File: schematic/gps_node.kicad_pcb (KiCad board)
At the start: 2 copper layers, 48 x 75 mm, 77 parts, among them IC2 MCP73831/2, J1 USB_OTG, J10 Mounting Hole, J11 TEST Vbatt, J12 Test 3.3v, J13 Test Gnd, J14 UART RF, J15 I2C GPS, J16 UART GPS, J17 GPIO_0, J18 GPIO_1, J2 AVR ICSP, J3 LIPO_BAT, J4 SOLAR, J5 FW_UPDATE, J6 SMA, J7 Mounting Hole, J8 Mounting Hole, J9 Mounting Hole, SW1 SW_SP3T, SW2 RESET, U1 TLV71333PDBV, U2 ublox-cam-m8q-0, U3 ATMEGA32U4-AU, U4 RN2483, Y1 16MHz

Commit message: First round of layout done
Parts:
- added IC1: MMA8452Q, gps_node_components:MMA8452Q, F.Cu at (124.7, 99.3)
- C10, C13, C20, C3, D1, D2, D5, F1, R1, R16, R17, R18, R19, R2: moved to B.Cu
- moved R19 98.9 mm to (128.3, 71.9), turned to 90 degrees
- moved C5 96.1 mm to (111.8, 95.8), turned to 270 degrees
- moved R10 94.6 mm to (121.9, 80.0)
- moved J12 93.3 mm to (109.2, 83.8)
- moved R18 93.1 mm to (131.3, 71.9), turned to 90 degrees
- moved R4 92.6 mm to (110.5, 80.3), turned to 90 degrees
- moved R3 89.5 mm to (112.5, 80.3), turned to 90 degrees
- moved C2 87.4 mm to (111.3, 108.0), turned to 90 degrees
- moved D8 87.2 mm to (115.6, 100.3), turned to 90 degrees
- moved D3 86.9 mm to (113.0, 90.2), turned to 90 degrees
- moved D7 85.5 mm to (113.8, 100.3), turned to 90 degrees
- moved J11 85.3 mm to (111.8, 116.8)
- moved C6 85.2 mm to (138.9, 85.1), turned to 270 degrees
- moved D2 84.7 mm to (108.7, 93.7), turned to 180 degrees
- moved D1 84.5 mm to (109.0, 87.4), turned to 90 degrees
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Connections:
- C18 pad 1: (no net) -> Net-(C18-Pad1)
- R16 pad 1: (no net) -> +BATT
- R8 pad 2: (no net) -> Net-(IC1-Pad9)
- R9 pad 2: (no net) -> Net-(IC1-Pad11)
- U4 pad 21: Net-(U4-Pad21) -> GND
- U4 pad 22: Net-(U4-Pad21) -> GND
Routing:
- net GND: track 0.00 -> 444.7 mm, vias 0 -> 43
- net +3V3: track 0.00 -> 187.8 mm, vias 0 -> 9
- net /I2C_GPS_SCL: track 0.00 -> 115.0 mm, vias 0 -> 2
- net /I2C_GPS_SDA: track 0.00 -> 106.0 mm, vias 0 -> 2
- net /UART_AT_TO_RN: track 0.00 -> 76.1 mm, vias 0 -> 3
- net /UART_RN_TO_AT: track 0.00 -> 70.9 mm, vias 0 -> 3
- net /UART_GPS_OUT: track 0.00 -> 65.8 mm, vias 0 -> 2
- net +BATT: track 0.00 -> 64.2 mm, vias 0 -> 3
- net /UART_GPS_IN: track 0.00 -> 61.6 mm
- net /MCU_PWSEL11_IN: track 0.00 -> 48.4 mm, vias 0 -> 3
- net /MCU_PWSEL0_IN: track 0.00 -> 46.2 mm, vias 0 -> 3
- net /RESET: track 0.00 -> 43.0 mm, vias 0 -> 1
- net /ACC_INT2: track 0.00 -> 42.6 mm, vias 0 -> 2
- net /MCU__OUT: track 0.00 -> 42.5 mm, vias 0 -> 2
- net /SCK: track 0.00 -> 40.5 mm, vias 0 -> 2
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- added copper zone on B.Cu, net GND
- added copper zone on F.Cu, net GND
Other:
- outline, holes or cut-outs redrawn

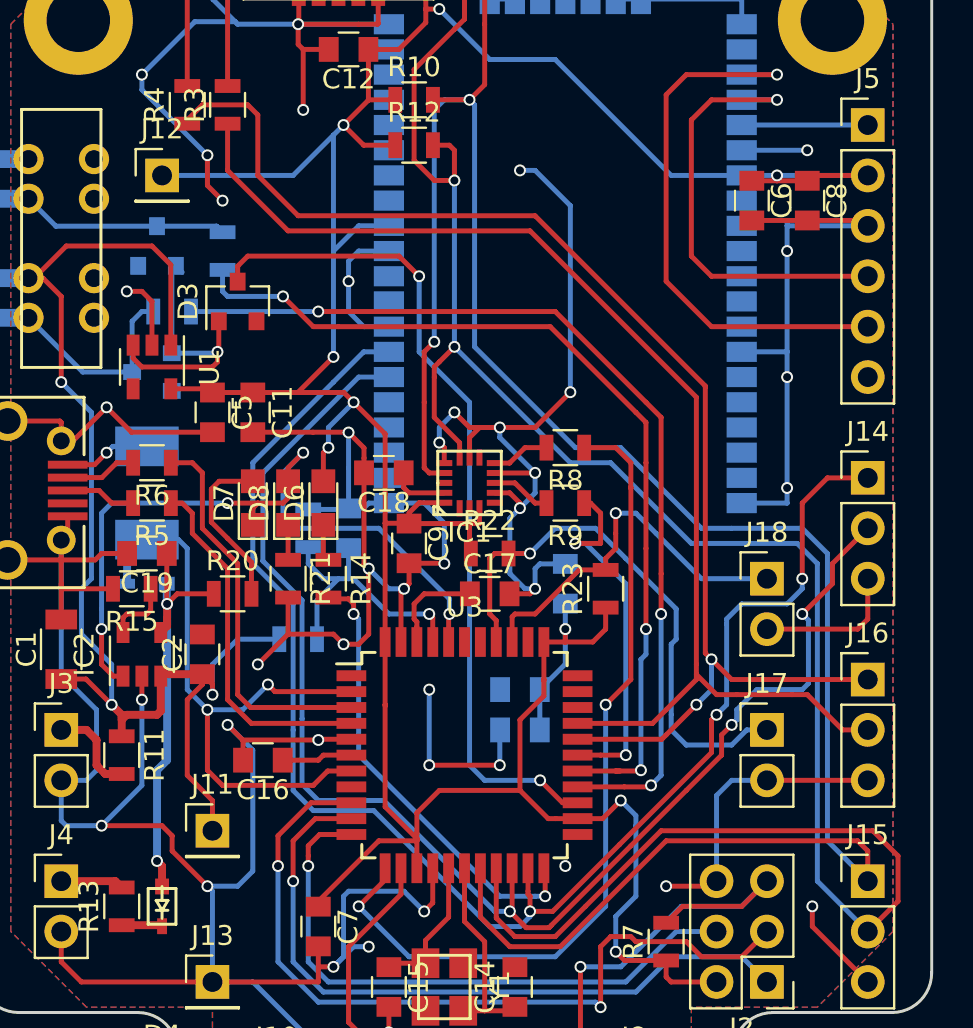
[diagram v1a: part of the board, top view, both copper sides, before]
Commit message: Issue #2: Adds RN2483 reset pin
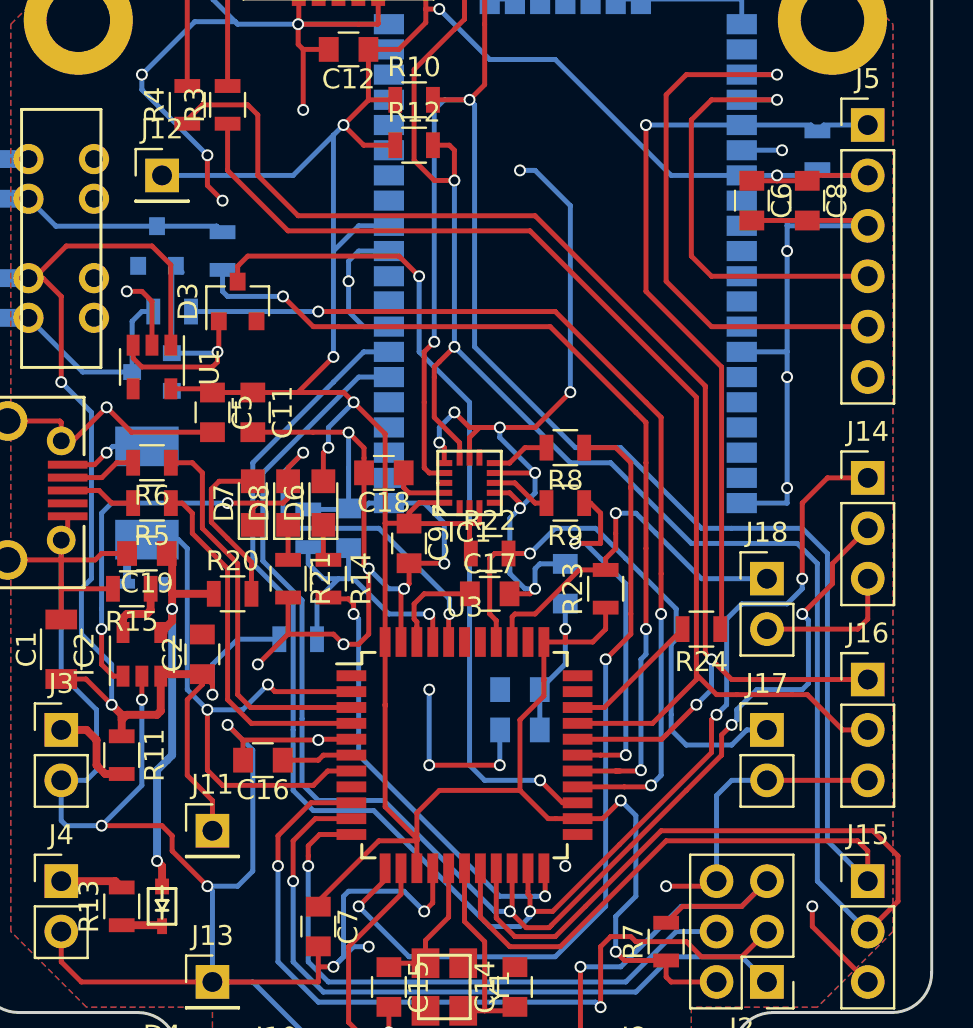
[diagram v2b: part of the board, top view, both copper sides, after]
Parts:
- added R24: 470, Resistors_SMD:R_0805, F.Cu at (136.4, 106.7)
- added R25: 10k, Resistors_SMD:R_0805, B.Cu at (142.2, 82.5)
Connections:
- net Net-(J5-Pad1) renamed /RN_RESET
- U3 pad 31: (no net) -> Net-(R24-Pad2)
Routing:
- net /RN_RESET: track 6.35 -> 38.4 mm, vias 0 -> 1
- net Net-(R24-Pad2): track 0.00 -> 6.92 mm
- net GND: track 444.7 -> 443.5 mm
- net /V_Charger: track 21.7 -> 22.8 mm
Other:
- net class Default: clearance 0.2 -> 0.17
- rule trace_clearance: 0.2 -> 0.17
- rule trace_min: 0.2 -> 0.16

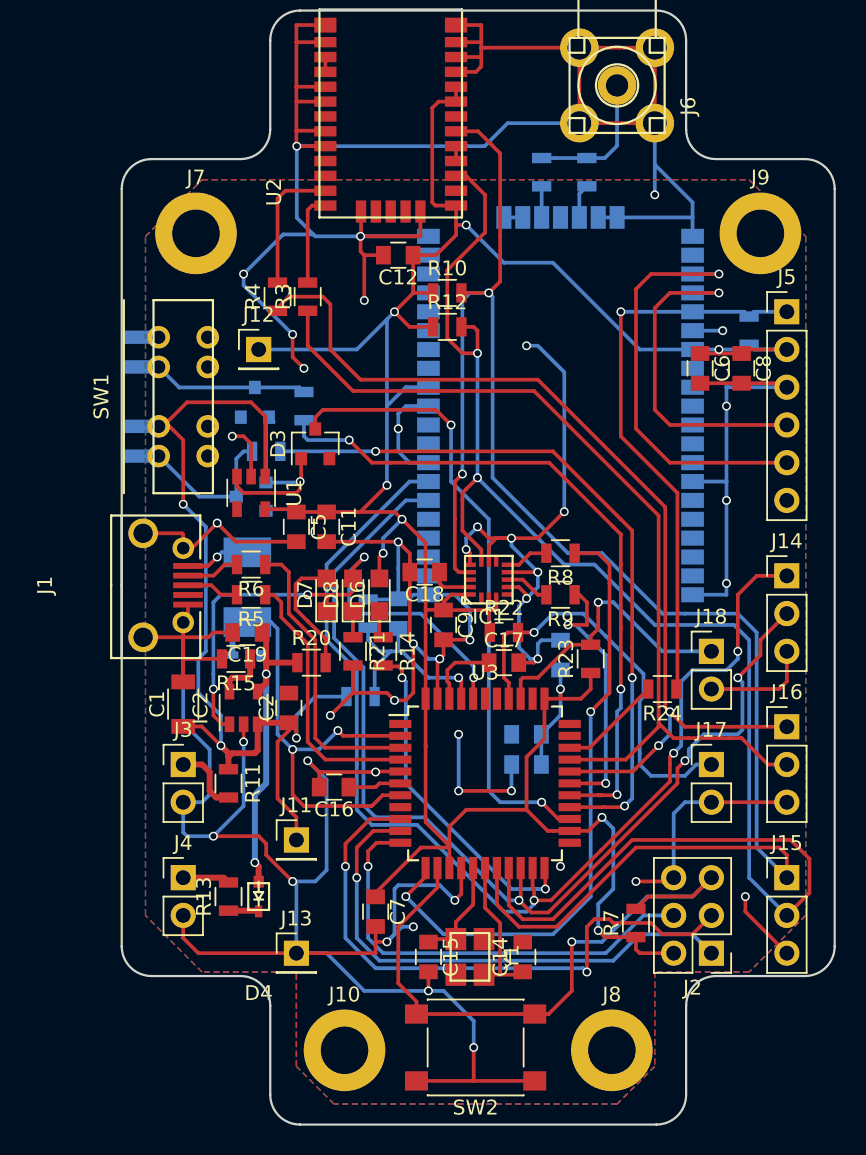
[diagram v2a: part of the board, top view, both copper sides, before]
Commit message: Adds RGB led, updates schematic
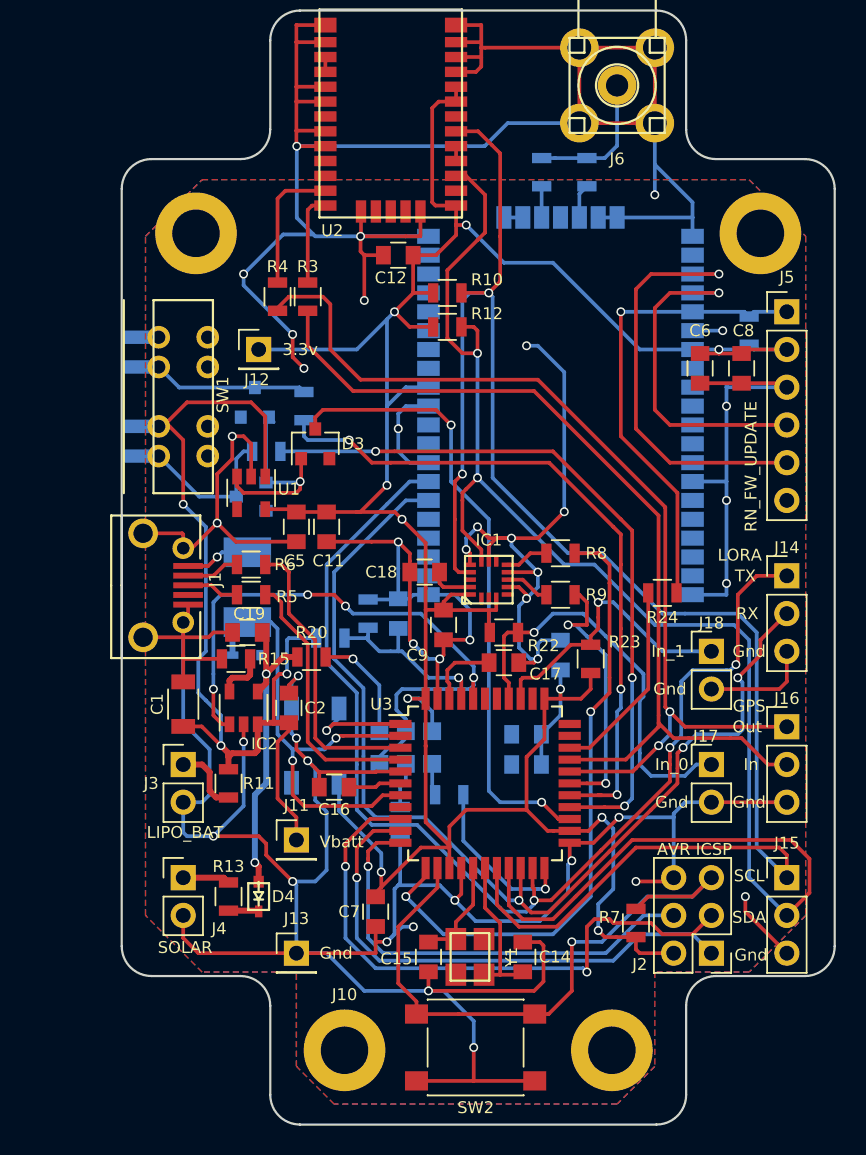
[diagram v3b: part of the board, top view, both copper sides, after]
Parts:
- added LED1: WS2812B, LEDs:LED_WS2812B-PLCC4, B.Cu at (113.0, 110.5)
- D6, D7, D8, R14, R21: moved to B.Cu
- J11: value TEST Vbatt -> Vbatt
- J12: value Test 3.3v -> 3.3v
- J13: value Test Gnd -> Gnd
- J5: value FW_UPDATE -> RN_FW_UPDATE
- moved R21 11.9 mm to (118.7, 115.6)
- moved D8 10.9 mm to (119.1, 110.6)
- moved D6 10.9 mm to (120.9, 110.6)
- moved D7 10.9 mm to (117.3, 110.6)
- moved R14 10.6 mm to (122.0, 113.8), turned to 0 degrees
- moved R24 6.48 mm to (136.4, 100.2)
- moved R16 4.43 mm to (114.0, 103.3)
- moved R20 0.38 mm to (112.8, 104.5)
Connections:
- IC1 pad 13: (no net) -> Net-(IC1-Pad13)
- IC1 pad 15: (no net) -> Net-(IC1-Pad15)
- IC1 pad 16: (no net) -> Net-(IC1-Pad16)
- IC1 pad 3: (no net) -> Net-(IC1-Pad3)
- IC1 pad 8: (no net) -> Net-(IC1-Pad8)
- J1 pad 4: (no net) -> Net-(J1-Pad4)
- J10 pad 1: (no net) -> Net-(J10-Pad1)
- J5 pad 6: (no net) -> Net-(J5-Pad6)
- J7 pad 1: (no net) -> Net-(J7-Pad1)
- J8 pad 1: (no net) -> Net-(J8-Pad1)
- J9 pad 1: (no net) -> Net-(J9-Pad1)
- U1 pad 4: (no net) -> Net-(U1-Pad4)
- U2 pad 2: (no net) -> Net-(U2-Pad2)
- U2 pad 20: (no net) -> Net-(U2-Pad20)
- U2 pad 23: (no net) -> Net-(U2-Pad23)
- U2 pad 24: (no net) -> Net-(U2-Pad24)
- U2 pad 28: (no net) -> Net-(U2-Pad28)
- U2 pad 29: (no net) -> Net-(U2-Pad29)
- U2 pad 30: (no net) -> Net-(U2-Pad30)
- U2 pad 7: (no net) -> Net-(U2-Pad7)
- U3 pad 1: (no net) -> /RGB_LED
- U3 pad 32: (no net) -> Net-(U3-Pad32)
- U3 pad 33: (no net) -> Net-(U3-Pad33)
- U3 pad 38: (no net) -> Net-(U3-Pad38)
- U3 pad 39: (no net) -> Net-(U3-Pad39)
- U3 pad 8: (no net) -> Net-(U3-Pad8)
- U4 pad 10: (no net) -> Net-(U4-Pad10)
- U4 pad 13: (no net) -> Net-(U4-Pad13)
- U4 pad 14: (no net) -> Net-(U4-Pad14)
- U4 pad 15: (no net) -> Net-(U4-Pad15)
- U4 pad 16: (no net) -> Net-(U4-Pad16)
- U4 pad 17: (no net) -> Net-(U4-Pad17)
- U4 pad 18: (no net) -> Net-(U4-Pad18)
- U4 pad 19: (no net) -> Net-(U4-Pad19)
- U4 pad 2: (no net) -> Net-(U4-Pad2)
- U4 pad 29: (no net) -> Net-(U4-Pad29)
- U4 pad 3: (no net) -> Net-(U4-Pad3)
- U4 pad 35: (no net) -> Net-(U4-Pad35)
- U4 pad 36: (no net) -> Net-(U4-Pad36)
- U4 pad 37: (no net) -> Net-(U4-Pad37)
- U4 pad 38: (no net) -> Net-(U4-Pad38)
- U4 pad 39: (no net) -> Net-(U4-Pad39)
- U4 pad 4: (no net) -> Net-(U4-Pad4)
- U4 pad 40: (no net) -> Net-(U4-Pad40)
- U4 pad 42: (no net) -> Net-(U4-Pad42)
- U4 pad 43: (no net) -> Net-(U4-Pad43)
- U4 pad 44: (no net) -> Net-(U4-Pad44)
- U4 pad 45: (no net) -> Net-(U4-Pad45)
- U4 pad 46: (no net) -> Net-(U4-Pad46)
- U4 pad 5: (no net) -> Net-(U4-Pad5)
- U4 pad 9: (no net) -> Net-(U4-Pad9)
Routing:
- net GND: track 443.5 -> 472.3 mm, vias 43 -> 41
- net /LED_OUT: track 22.9 -> 11.4 mm, vias 2 -> 1
- net +3V3: track 188.1 -> 196.2 mm, vias 9 -> 10
- net /RGB_LED: track 0.00 -> 6.98 mm, vias 0 -> 1
- net /RN_RESET: track 38.4 -> 32.0 mm
- net Net-(R24-Pad2): track 6.92 -> 13.4 mm
- net /charge_status: track 38.6 -> 42.8 mm
- net /BAT_MEASURE: track 14.5 -> 12.6 mm
- net +BATT: track 64.2 -> 65.8 mm
- net Net-(D8-Pad1): track 1.76 -> 3.06 mm
- net Net-(D7-Pad2): track 8.37 -> 7.60 mm, vias 0 -> 1
- net (no net): vias 1 -> 0
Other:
- board text added: "GPS"
- board text added: "Gnd"
- board text added: "In"
- board text added: "In_0"
- board text added: "In_1"
- board text added: "LORA"
- board text added: "Out"
- board text added: "RX"
- board text added: "SCL"
- board text added: "SDA"
- board text added: "TX"

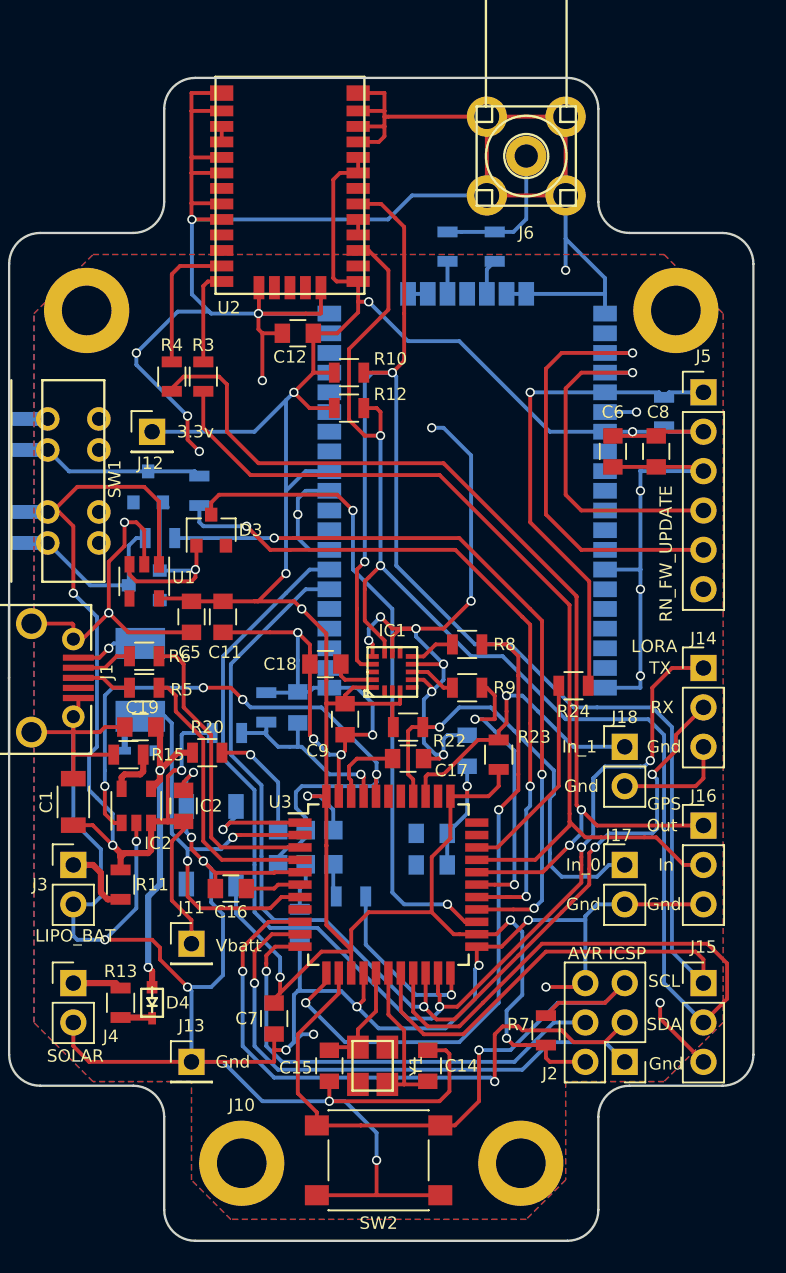
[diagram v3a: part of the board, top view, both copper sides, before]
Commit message: Added more group pour aroudd gps, additional buttons
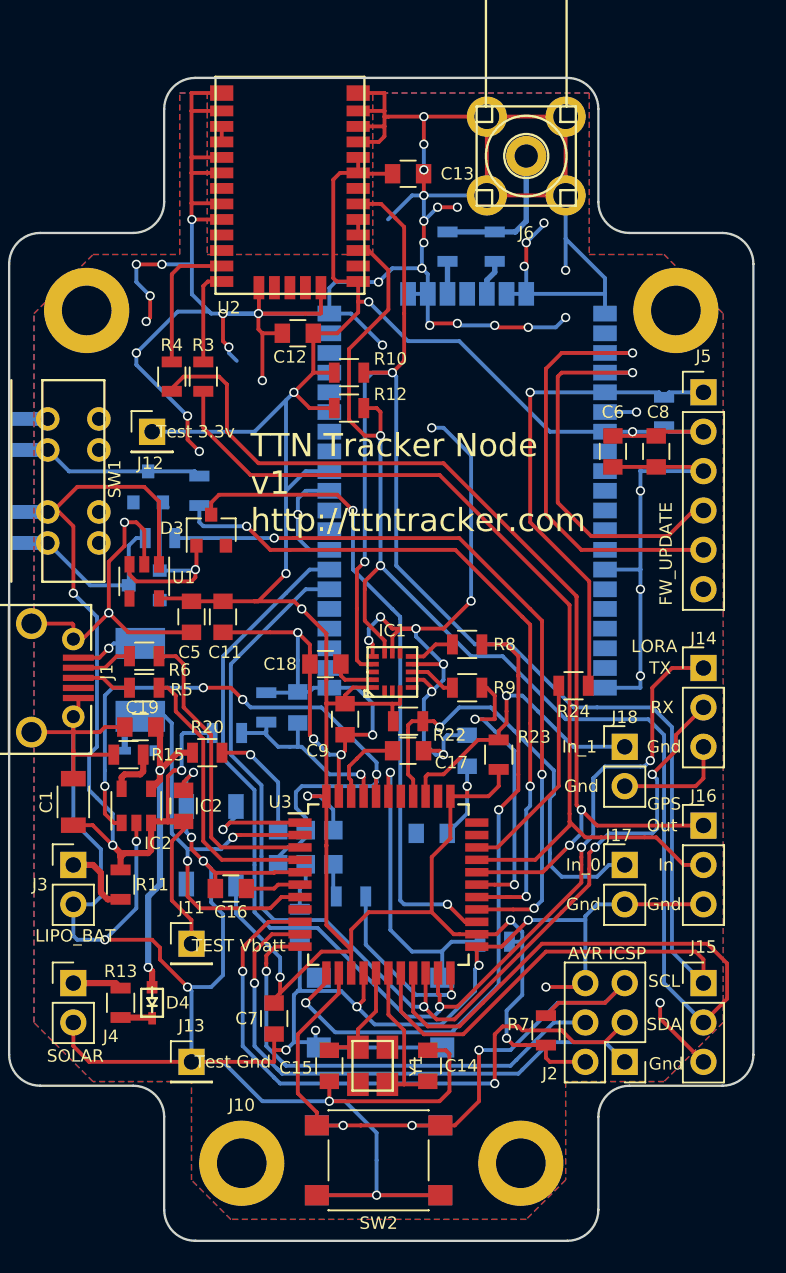
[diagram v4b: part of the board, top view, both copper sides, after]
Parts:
- added R26: 4.7k, Resistors_SMD:R_0805, B.Cu at (131.3, 116.7)
- added SW3: RESET, Buttons_Switches_SMD:SW_SPST_PTS645, B.Cu at (123.8, 130.8)
- added SW4: RESET, Buttons_Switches_SMD:SW_SPST_PTS645, B.Cu at (124.0, 121.3)
- C13: moved to F.Cu
- J11: value Vbatt -> TEST Vbatt
- J12: value 3.3v -> Test 3.3v
- J13: value Gnd -> Test Gnd
- J5: value RN_FW_UPDATE -> FW_UPDATE
- moved C13 44.6 mm to (125.7, 67.2), turned to 0 degrees
- moved C17 0.51 mm to (125.7, 104.4)
- moved R22 0.38 mm to (125.7, 102.5)
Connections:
- U3 pad 39: Net-(U3-Pad39) -> /BUTTON_1
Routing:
- net GND: track 472.3 -> 532.2 mm, vias 41 -> 66
- net /BUTTON_1: track 0.00 -> 20.1 mm, vias 0 -> 1
- net /RESET: track 43.0 -> 46.5 mm, vias 1 -> 3
- net Net-(J5-Pad4): track 22.7 -> 25.8 mm
- net /ACC_INT2: track 42.6 -> 41.5 mm
- net +3V3: track 196.2 -> 197.3 mm
- net /IN_0: track 27.7 -> 28.3 mm
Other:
- net class 50_OHM_line added: clearance 0.12, trace_width 0.35, via_dia 0.6, via_drill 0.4
- board text added: "TTN Tracker Node v1 http://ttntracker.com"
